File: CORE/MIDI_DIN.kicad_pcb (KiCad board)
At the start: 2 copper layers, 29.5 x 99.8 mm, 56 parts, among them J1 Conn_02x08_Odd_Even, J2 USB_C_Receptacle_USB2.0, J3 Conn_01x04, J5 DIN-5_180degree, J6 DIN-5_180degree, J7 Conn_01x06, Q1 MMBT3904, SW1 SW_SPDT, SW2 SW_Push_DPDT, U1 ATSAMD21G15B-A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

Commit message: Fix DRC errors
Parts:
- moved C15 0.71 mm to (100.0, 67.5), turned to 45 degrees
- moved U4 0.50 mm to (98.0, 61.5)
- moved Y1 0.50 mm to (95.8, 56.5)
- moved C13 0.25 mm to (92.2, 55.8)
- moved C14 0.25 mm to (94.8, 53.2)
- moved C7 0.25 mm to (91.0, 69.2)
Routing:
- net Net-(C13-Pad1): track 5.18 -> 6.16 mm
- net +3V3: track 38.0 -> 37.3 mm
- net Net-(U4-Pad2): track 11.2 -> 11.7 mm
- net SPI_SS: track 16.3 -> 15.8 mm
- net SPI_MOSI: track 17.9 -> 17.4 mm

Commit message: Add custom symbols and footprints
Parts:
- C16: value 22nF -> 4.7nF
- J1: footprint CustomLib:Header_2x8_Shrouded_SMD -> Custom_FP:Header_2x8_Shrouded_SMD
- J2: footprint CustomLib:USB_C_Receptacle_GCT_USB4085_Slimmed -> Custom_FP:USB_C_Receptacle_GCT_USB4085_Slimmed
- J3: footprint CustomLib:MicroMatch_04_Vertical_SMD -> Custom_FP:MicroMatch_04_Vertical_SMD
- J5, J6: value DIN-5_180degree -> MAB5100S; footprint CustomLib:DIN-5_Hirschmann -> Custom_FP:DIN-5_Hirschmann_MAB5100S
- R18, R19: value 120 -> 56
- SW1: footprint CustomLib:SlideSwitch-SS12D10 -> Custom_FP:SlideSwitch-SS12D10
- SW2: footprint CustomLib:SlideDPDT_JS202011 -> Custom_FP:SlideDPDT_JS202011
- Y1: footprint CustomLib:Crystal_2pin_2.0x2.5mm -> Custom_FP:Crystal_2pin_2.0x2.5mm
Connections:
- J1 pad 1: (no net) -> Net-(J1-Pad1)
- J1 pad 10: (no net) -> Net-(J1-Pad10)
- J1 pad 13: (no net) -> Net-(J1-Pad13)
- J1 pad 14: (no net) -> Net-(J1-Pad14)
- J1 pad 15: (no net) -> Net-(J1-Pad15)
- J1 pad 16: (no net) -> Net-(J1-Pad16)
- J1 pad 2: (no net) -> Net-(J1-Pad2)
- J1 pad 9: (no net) -> Net-(J1-Pad9)
- J2 pad A8: (no net) -> Net-(J2-PadA8)
- J2 pad B8: (no net) -> Net-(J2-PadB8)
- J5 pad 1: (no net) -> Net-(J5-Pad1)
- J5 pad 2: (no net) -> Net-(J5-Pad2)
- J5 pad 3: (no net) -> Net-(J5-Pad3)
- J6 pad 1: (no net) -> Net-(J6-Pad1)
- J6 pad 3: (no net) -> Net-(J6-Pad3)
- J7 pad 6: (no net) -> Net-(J7-Pad6)
- SW2 pad 3: (no net) -> Net-(SW2-Pad3)
- SW2 pad 6: (no net) -> Net-(SW2-Pad6)
- U1 pad 1: (no net) -> Net-(U1-Pad1)
- U1 pad 10: (no net) -> Net-(U1-Pad10)
- U1 pad 11: (no net) -> Net-(U1-Pad11)
- U1 pad 12: (no net) -> Net-(U1-Pad12)
- U1 pad 19: (no net) -> Net-(U1-Pad19)
- U1 pad 20: (no net) -> Net-(U1-Pad20)
- U1 pad 22: (no net) -> Net-(U1-Pad22)
- U1 pad 24: (no net) -> Net-(U1-Pad24)
- U1 pad 25: (no net) -> Net-(U1-Pad25)
- U1 pad 27: (no net) -> Net-(U1-Pad27)
- U1 pad 29: (no net) -> Net-(U1-Pad29)
- U1 pad 3: (no net) -> Net-(U1-Pad3)
- U1 pad 31: (no net) -> Net-(U1-Pad31)
- U1 pad 32: (no net) -> Net-(U1-Pad32)
- U1 pad 37: (no net) -> Net-(U1-Pad37)
- U1 pad 38: (no net) -> Net-(U1-Pad38)
- U1 pad 39: (no net) -> Net-(U1-Pad39)
- U1 pad 4: (no net) -> Net-(U1-Pad4)
- U1 pad 41: (no net) -> Net-(U1-Pad41)
- U1 pad 47: (no net) -> Net-(U1-Pad47)
- U1 pad 48: (no net) -> Net-(U1-Pad48)
- U1 pad 7: (no net) -> Net-(U1-Pad7)
- U1 pad 8: (no net) -> Net-(U1-Pad8)
- U1 pad 9: (no net) -> Net-(U1-Pad9)
- U2 pad 3: (no net) -> Net-(U2-Pad3)
- U3 pad 4: (no net) -> Net-(U3-Pad4)
- U4 pad 3: (no net) -> Net-(U4-Pad3)
- U4 pad 8: (no net) -> Net-(U4-Pad8)
- U4 pad 9: (no net) -> Net-(U4-Pad9)

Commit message: Update PCB
Fixed stuff
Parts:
- added R17: 10k, Resistor_SMD:R_0603_1608Metric, B.Cu at (88.8, 70.5)
- added SW3: PROG, Custom_FP:Tactile_angled_5x5.4_SMD, F.Cu at (100.0, 114.5)
- added SW4: SW_DIP_x04, Button_Switch_SMD:SW_DIP_SPSTx04_Slide_Copal_CHS-04B_W7.62mm_P1.27mm, F.Cu at (99.5, 71.8)
- added SW5: RST, Custom_FP:Tactile_angled_5x5.4_SMD, F.Cu at (100.0, 105.8)
- J2: footprint Custom_FP:USB_C_Receptacle_GCT_USB4085_Slimmed -> Connector_USB:USB_C_Receptacle_HRO_TYPE-C-31-M-12
- Q1: value MMBT3904 -> MMBT3906
- R3, R5: moved to F.Cu
- moved R9 14.8 mm to (85.5, 129.0), turned to 0 degrees
- moved R12 13.8 mm to (80.0, 61.2), turned to 270 degrees
- moved R5 5.64 mm to (85.8, 75.2), turned to 90 degrees
- moved J2 5.41 mm to (79.5, 72.8)
- moved Q1 3.29 mm to (81.2, 127.2), turned to 0 degrees
- moved R3 3.26 mm to (85.8, 70.2), turned to 270 degrees
- moved R7 1.00 mm to (77.5, 128.2)
- moved C4 0.71 mm to (88.8, 76.0)
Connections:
- Q1 pad 2: GND -> +3V3
- R10 pad 2: Net-(Q1-Pad3) -> GND
- R9 pad 1: +3V3 -> Net-(Q1-Pad3)
- U1 pad 41: Net-(U1-Pad41) -> PROG
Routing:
- net PROG: track 0.00 -> 63.4 mm, vias 0 -> 1
- net RST: track 18.7 -> 71.2 mm, vias 1 -> 3
- net Net-(SW4-Pad6): track 0.00 -> 10.6 mm, vias 0 -> 1
- net Net-(SW4-Pad5): track 0.00 -> 10.3 mm, vias 0 -> 1
- net VBUS: track 45.5 -> 40.7 mm, vias 2 -> 3
- net Net-(J6-Pad4): track 4.89 -> 9.34 mm
- net Net-(SW4-Pad8): track 0.00 -> 4.16 mm, vias 0 -> 1
- net Net-(SW4-Pad7): track 0.00 -> 3.65 mm, vias 0 -> 1
- net Net-(Q1-Pad3): track 5.77 -> 3.19 mm
- net +3V3: track 37.3 -> 39.4 mm, vias 2 -> 1
- net USB_D-: track 15.4 -> 17.1 mm
- net Net-(C2-Pad1): track 21.9 -> 20.3 mm
- net Net-(Q1-Pad1): track 3.44 -> 1.98 mm
- net Net-(J5-Pad4): track 20.4 -> 19.0 mm
- net +5V: track 74.6 -> 75.7 mm
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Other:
- board text added: "MIDIBUS_DIN V2.1 GuavTek"
- board text added: "PROG"
- board text added: "RST"
- board text removed: "MIDIBUS_DIN V2.0 GuavTek"

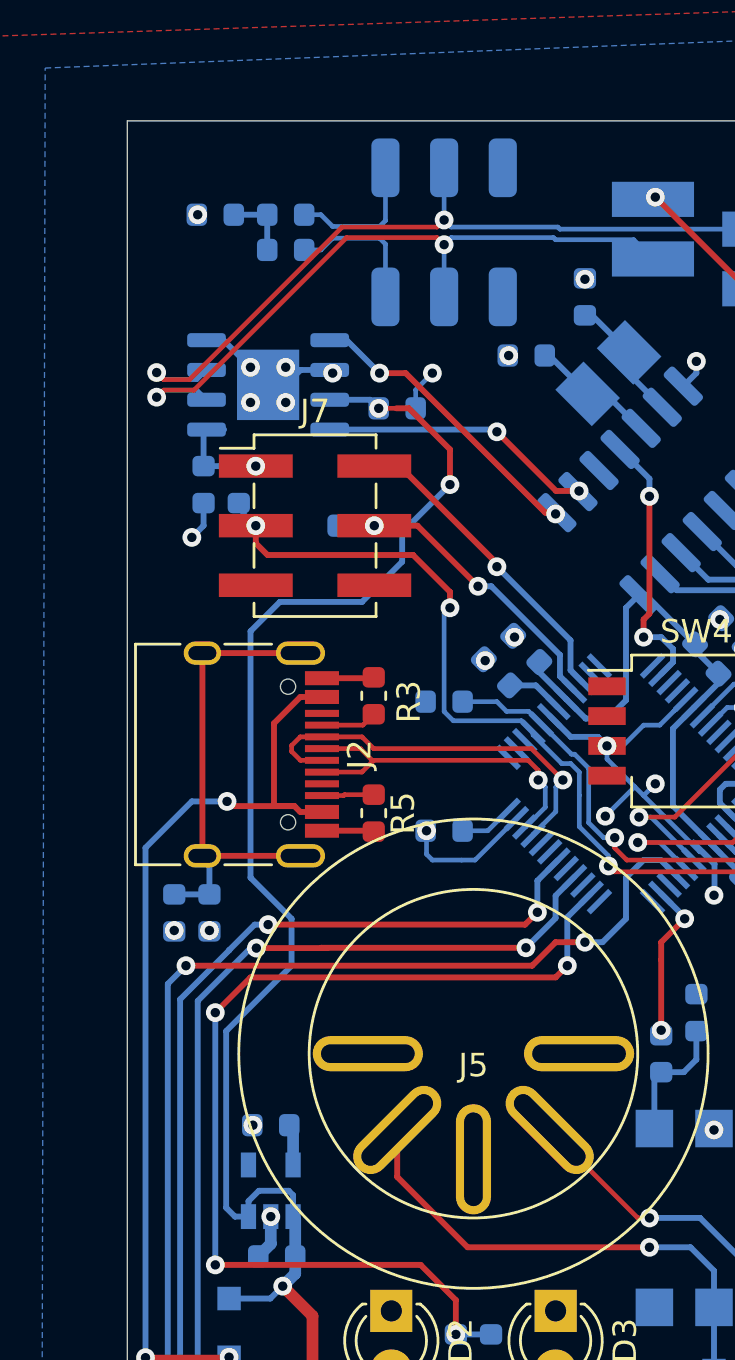
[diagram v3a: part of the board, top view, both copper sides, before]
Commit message: Add horizontal prog header
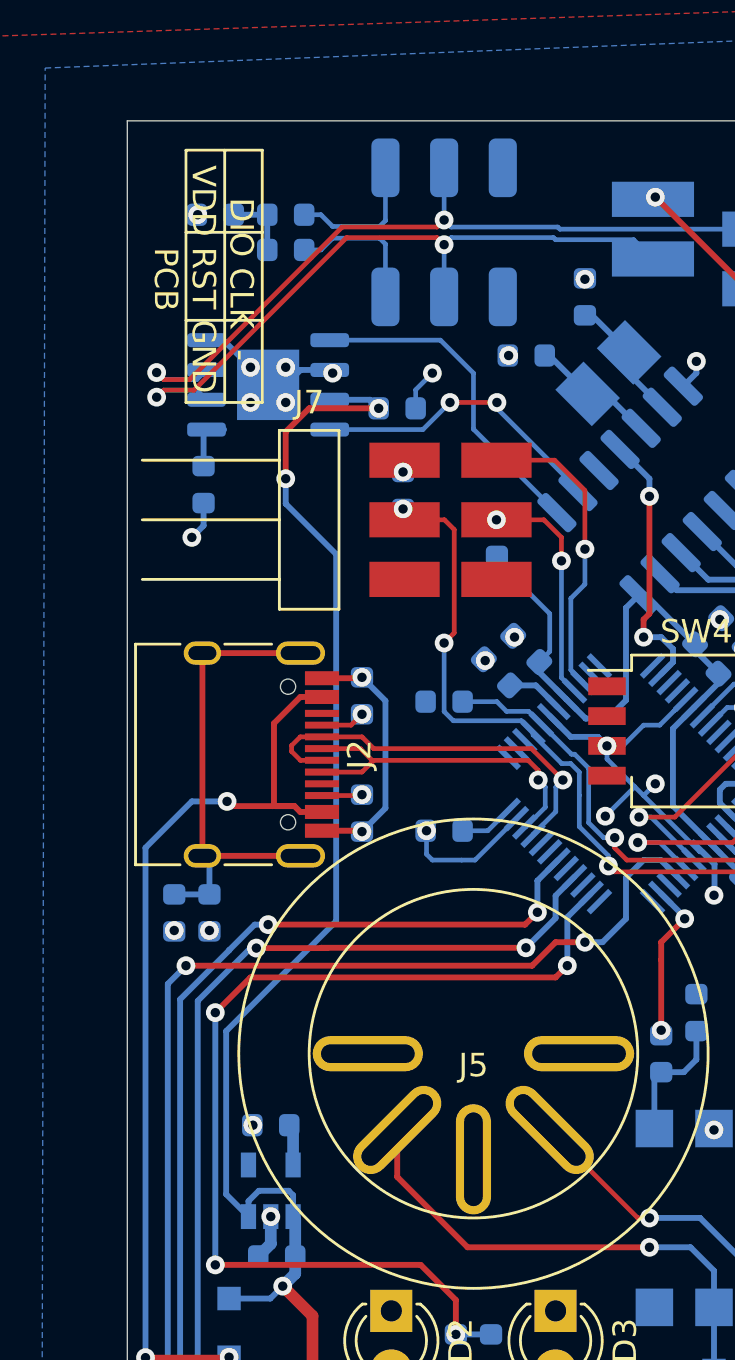
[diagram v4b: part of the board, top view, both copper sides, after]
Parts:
- J7: footprint Connector_PinHeader_2.54mm:PinHeader_2x03_P2.54mm_Vertical_SMD -> Custom_FP:TSM103-DH
- R3, R5: moved to B.Cu
- moved R12 7.00 mm to (87.0, 61.5)
- moved R15 6.02 mm to (91.0, 63.5), turned to 90 degrees
- moved R3 0.50 mm to (85.2, 70.2)
- moved R5 0.50 mm to (85.2, 75.2)
- moved J7 0.35 mm to (83.0, 62.8)
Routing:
- net GND: track 38.3 -> 45.7 mm, vias 54 -> 56
- net RST: track 71.2 -> 65.6 mm
- net +3V3: track 39.4 -> 43.3 mm
- net +5V: track 75.7 -> 72.1 mm
- net SWCLK: track 12.0 -> 9.90 mm
- net Net-(U4-Pad1): track 12.7 -> 14.1 mm, vias 2 -> 0
- net Net-(U4-Pad2): track 11.7 -> 12.8 mm
- net SWDIO: track 13.5 -> 13.0 mm
- net Net-(J2-PadB5): track 2.22 -> 1.72 mm, vias 0 -> 1
- net Net-(J2-PadA5): track 2.40 -> 1.90 mm, vias 0 -> 1
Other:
- board text added: "DIO CLK - VDD RST GND PCB"

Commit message: Minor adjustments
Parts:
- R18, R19: value 56 -> 62
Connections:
- J1 pad 1: Net-(J1-Pad1) -> (no net)
- J1 pad 10: Net-(J1-Pad10) -> (no net)
- J1 pad 13: Net-(J1-Pad13) -> (no net)
- J1 pad 14: Net-(J1-Pad14) -> (no net)
- J1 pad 15: Net-(J1-Pad15) -> (no net)
- J1 pad 16: Net-(J1-Pad16) -> (no net)
- J1 pad 2: Net-(J1-Pad2) -> (no net)
- J1 pad 9: Net-(J1-Pad9) -> (no net)
- J2 pad A8: Net-(J2-PadA8) -> (no net)
- J2 pad B8: Net-(J2-PadB8) -> (no net)
- J5 pad 1: Net-(J5-Pad1) -> (no net)
- J5 pad 2: Net-(J5-Pad2) -> (no net)
- J5 pad 3: Net-(J5-Pad3) -> (no net)
- J6 pad 1: Net-(J6-Pad1) -> (no net)
- J6 pad 3: Net-(J6-Pad3) -> (no net)
- J7 pad 6: Net-(J7-Pad6) -> (no net)
- SW2 pad 3: Net-(SW2-Pad3) -> (no net)
- SW2 pad 6: Net-(SW2-Pad6) -> (no net)
- U1 pad 1: Net-(U1-Pad1) -> (no net)
- U1 pad 10: Net-(U1-Pad10) -> (no net)
- U1 pad 11: Net-(U1-Pad11) -> (no net)
- U1 pad 12: Net-(U1-Pad12) -> (no net)
- U1 pad 22: Net-(U1-Pad22) -> (no net)
- U1 pad 24: Net-(U1-Pad24) -> (no net)
- U1 pad 25: Net-(U1-Pad25) -> (no net)
- U1 pad 27: Net-(U1-Pad27) -> (no net)
- U1 pad 29: Net-(U1-Pad29) -> (no net)
- U1 pad 3: Net-(U1-Pad3) -> (no net)
- U1 pad 31: Net-(U1-Pad31) -> (no net)
- U1 pad 32: Net-(U1-Pad32) -> (no net)
- U1 pad 37: Net-(U1-Pad37) -> (no net)
- U1 pad 38: Net-(U1-Pad38) -> (no net)
- U1 pad 39: Net-(U1-Pad39) -> (no net)
- U1 pad 4: Net-(U1-Pad4) -> (no net)
- U1 pad 47: Net-(U1-Pad47) -> (no net)
- U1 pad 48: Net-(U1-Pad48) -> (no net)
- U1 pad 9: Net-(U1-Pad9) -> (no net)
- U2 pad 3: Net-(U2-Pad3) -> (no net)
- U3 pad 4: Net-(U3-Pad4) -> (no net)
- U4 pad 3: Net-(U4-Pad3) -> (no net)
- U4 pad 8: Net-(U4-Pad8) -> (no net)
- U4 pad 9: Net-(U4-Pad9) -> (no net)
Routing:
- net PROG: track 63.4 -> 62.9 mm
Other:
- board text added: "DOWN = ON 1 2 4 8"

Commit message: Update sheet metadata
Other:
- board text added: "M2IDI_DIN V2.1 GuavTek"
- board text removed: "MIDIBUS_DIN V2.1 GuavTek"
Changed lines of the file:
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@@
   )
   (page A4)
+  (title_block
+    (title "M2IDI - DIN")
+    (date 2023-03-17)
+    (rev 2.1)
+  )
   (layers
     (0 F.Cu signal)
@@
   )
   (gr_line (start 86.21 54.826) (end 86.21 55.334) (layer B.SilkS) (width 0.12))
-  (gr_text "MIDIBUS_DIN\nV2.1\nGuavTek" (at 90 104.75) (layer F.SilkS)
+  (gr_text "M2IDI_DIN\nV2.1\nGuavTek" (at 90 104.75) (layer F.SilkS)
     (effects (font (size 1 1) (thickness 0.15)))
   )

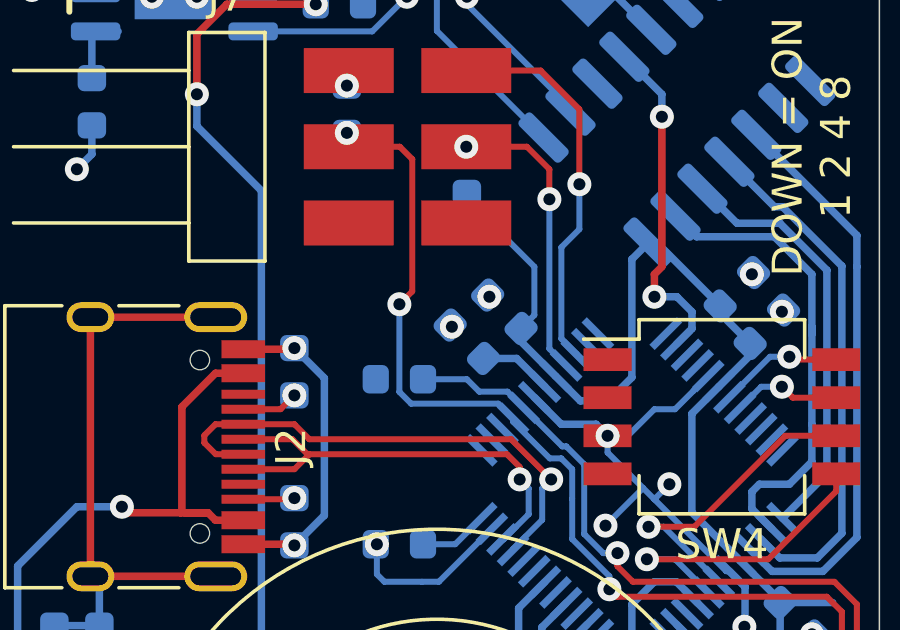
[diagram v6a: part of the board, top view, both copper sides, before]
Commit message: Move resistor out of the way
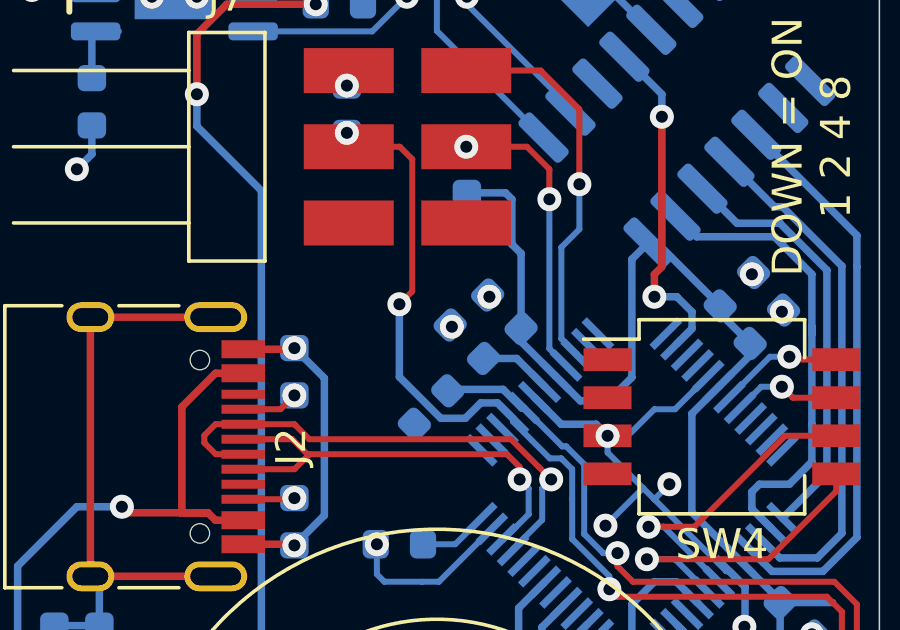
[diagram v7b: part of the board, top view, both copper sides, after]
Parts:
- moved R17 1.42 mm to (89.8, 71.4), turned to 45 degrees
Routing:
- net +3V3: track 43.3 -> 44.3 mm
- net PROG: track 62.9 -> 62.0 mm
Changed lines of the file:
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@@
     (thickness 1.6)
     (drawings 24)
-    (tracks 538)
+    (tracks 543)
     (zones 0)
     (modules 60)
@@
   )
   (module Resistor_SMD:R_0603_1608Metric (layer B.Cu)
-    (at 88.75 70.5)
+    (at 89.806847 71.443153 45)
     (descr "Resistor SMD 0603 (1608 Metric), square (rectangular) end terminal, IPC_7351 nominal, (Body size source: http://www.tortai-tech.com/upload/download/2011102023233369053.pdf), generated with kicad-footprint-generator")
     (tags resistor)
     (attr smd)
-    (fp_text reference R17 (at 0 1.43) (layer B.SilkS)
+    (fp_text reference R17 (at -0.080394 -1.414214 45) (layer B.SilkS)
       (effects (font (size 1 1) (thickness 0.15)) (justify mirror))
     )
-    (fp_text value 10k (at 0 -1.43) (layer B.Fab)
+    (fp_text value 10k (at 0 -1.43 45) (layer B.Fab)
       (effects (font (size 1 1) (thickness 0.15)) (justify mirror))
     )
@@
     (fp_line (start 1.48 0.73) (end 1.48 -0.73) (layer B.CrtYd) (width 0.05))
     (fp_line (start 1.48 -0.73) (end -1.48 -0.73) (layer B.CrtYd) (width 0.05))
-    (fp_text user %R (at 0 0) (layer B.Fab)
+    (fp_text user %R (at 0 0 45) (layer B.Fab)
       (effects (font (size 0.4 0.4) (thickness 0.06)) (justify mirror))
     )
-    (pad 2 smd roundrect (at 0.7875 0) (size 0.875 0.95) (layers B.Cu B.Paste B.Mask) (roundrect_rratio 0.25)
+    (pad 2 smd roundrect (at 0.7875 0 45) (size 0.875 0.95) (layers B.Cu B.Paste B.Mask) (roundrect_rratio 0.25)
       (net 47 PROG))
-    (pad 1 smd roundrect (at -0.7875 0) (size 0.875 0.95) (layers B.Cu B.Paste B.Mask) (roundrect_rratio 0.25)
+    (pad 1 smd roundrect (at -0.7875 0 45) (size 0.875 0.95) (layers B.Cu B.Paste B.Mask) (roundrect_rratio 0.25)
       (net 17 +3V3))
     (model ${KISYS3DMOD}/Resistor_SMD.3dshapes/R_0603_1608Metric.wrl
@@
   (segment (start 87.064 60.6485) (end 87 60.7125) (width 0.2) (layer F.Cu) (net 17))
   (segment (start 87.064 60.21) (end 87.064 60.6485) (width 0.2) (layer F.Cu) (net 17))
-  (segment (start 93.25 68.363694) (end 92.806847 68.806847) (width 0.2) (layer B.Cu) (net 17))
-  (segment (start 93.25 66.75) (end 93.25 68.363694) (width 0.2) (layer B.Cu) (net 17))
-  (segment (start 91 64.5) (end 93.25 66.75) (width 0.2) (layer B.Cu) (net 17))
   (segment (start 91 64.2875) (end 91 64.5) (width 0.2) (layer B.Cu) (net 17))
+  (segment (start 92.806847 68.806847) (end 92.806847 66.306847) (width 0.25) (layer B.Cu) (net 17))
+  (segment (start 91 64.2875) (end 92.2875 64.2875) (width 0.25) (layer B.Cu) (net 17))
+  (segment (start 92.2875 64.2875) (end 92.5 64.5) (width 0.25) (layer B.Cu) (net 17))
+  (segment (start 92.5 64.5) (end 92.5 66) (width 0.25) (layer B.Cu) (net 17))
+  (segment (start 92.5 66) (end 92.25 65.75) (width 0.25) (layer B.Cu) (net 17))
+  (segment (start 92.806847 66.306847) (end 92.5 66) (width 0.25) (layer B.Cu) (net 17))
   (segment (start 77.25 78.7125) (end 78.75 78.7125) (width 0.25) (layer B.Cu) (net 18))
   (segment (start 78.45 68.43) (end 78.45 77.07) (width 0.25) (layer F.Cu) (net 18))
@@
   (segment (start 88.764 62.75) (end 89.179999 63.165999) (width 0.2) (layer F.Cu) (net 29))
   (segment (start 87.064 62.75) (end 88.764 62.75) (width 0.2) (layer F.Cu) (net 29))
-  (segment (start 89.142364 71.313504) (end 92.045737 71.313504) (width 0.2) (layer B.Cu) (net 29))
-  (segment (start 88.75 70.92114) (end 89.142364 71.313504) (width 0.2) (layer B.Cu) (net 29))
-  (segment (start 92.045737 71.313504) (end 92.540202 71.807969) (width 0.2) (layer B.Cu) (net 29))
-  (segment (start 88.75 68) (end 88.75 70.92114) (width 0.2) (layer B.Cu) (net 29))
   (segment (start 98.3 105.05) (end 98.3 102.85) (width 0.2) (layer F.Cu) (net 29))
   (segment (start 103.25 105.75) (end 99 105.75) (width 0.2) (layer F.Cu) (net 29))
@@
   (segment (start 99 105.75) (end 98.3 105.05) (width 0.2) (layer F.Cu) (net 29))
   (segment (start 95.75 77.5) (end 96 77.75) (width 0.2) (layer F.Cu) (net 29))
+  (segment (start 92.020737 71.288504) (end 92.540202 71.807969) (width 0.25) (layer B.Cu) (net 29))
+  (segment (start 91.461496 71.288504) (end 92.020737 71.288504) (width 0.25) (layer B.Cu) (net 29))
+  (segment (start 90.948718 71.801282) (end 91.461496 71.288504) (width 0.25) (layer B.Cu) (net 29))
+  (segment (start 88.75 70.421646) (end 90.129636 71.801282) (width 0.25) (layer B.Cu) (net 29))
+  (segment (start 90.129636 71.801282) (end 90.948718 71.801282) (width 0.25) (layer B.Cu) (net 29))
+  (segment (start 88.75 68) (end 88.75 70.421646) (width 0.25) (layer B.Cu) (net 29))
   (segment (start 97.71 86.5775) (end 98 86.2875) (width 0.25) (layer B.Cu) (net 30))
   (segment (start 97.71 88.69) (end 97.71 86.5775) (width 0.25) (layer B.Cu) (net 30))
@@
   (segment (start 89.25 96) (end 87.75 94.5) (width 0.25) (layer F.Cu) (net 46))
   (segment (start 89.25 97.4625) (end 89.25 96) (width 0.25) (layer F.Cu) (net 46))
-  (segment (start 92.352833 70.913494) (end 92.893755 71.454416) (width 0.2) (layer B.Cu) (net 47))
-  (segment (start 91.413494 70.913494) (end 92.352833 70.913494) (width 0.2) (layer B.Cu) (net 47))
-  (segment (start 91 70.5) (end 91.413494 70.913494) (width 0.2) (layer B.Cu) (net 47))
-  (segment (start 89.5375 70.5) (end 91 70.5) (width 0.2) (layer B.Cu) (net 47))
   (segment (start 94.910122 73.336724) (end 94.910122 75.660122) (width 0.2) (layer B.Cu) (net 47))
   (segment (start 94.177742 72.738403) (end 94.311801 72.738403) (width 0.2) (layer B.Cu) (net 47))
@@
   (segment (start 99.25 114.25) (end 98.3 113.3) (width 0.2) (layer F.Cu) (net 47))
   (segment (start 96.020274 76.296414) (end 96.020274 76.734272) (width 0.2) (layer F.Cu) (net 47))
+  (segment (start 90.411506 70.838494) (end 90.363694 70.886306) (width 0.25) (layer B.Cu) (net 47))
+  (segment (start 92.207137 70.838494) (end 90.411506 70.838494) (width 0.25) (layer B.Cu) (net 47))
+  (segment (start 92.823061 71.454416) (end 92.207137 70.838494) (width 0.25) (layer B.Cu) (net 47))
+  (segment (start 92.893755 71.454416) (end 92.823061 71.454416) (width 0.25) (layer B.Cu) (net 47))
   (via (at 101.75 69.75) (size 0.8) (drill 0.4) (layers F.Cu B.Cu) (net 48))
   (segment (start 101.103553 69.75) (end 101.75 69.75) (width 0.2) (layer B.Cu) (net 48))
